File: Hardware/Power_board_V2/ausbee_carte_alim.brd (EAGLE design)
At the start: 97.1 x 71.4 mm, 27 parts, among them K1 G5LE

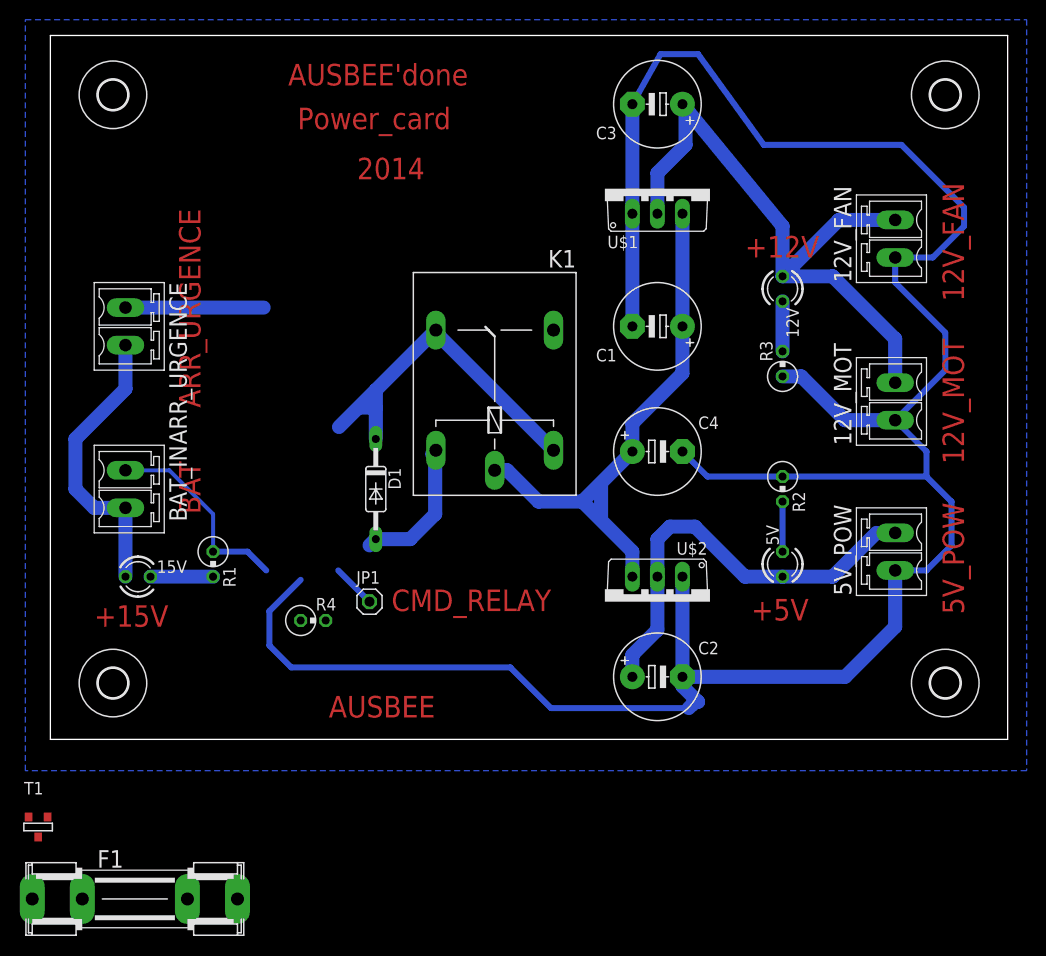
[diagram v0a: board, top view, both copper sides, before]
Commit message: Power board V2, adaptator GPIO
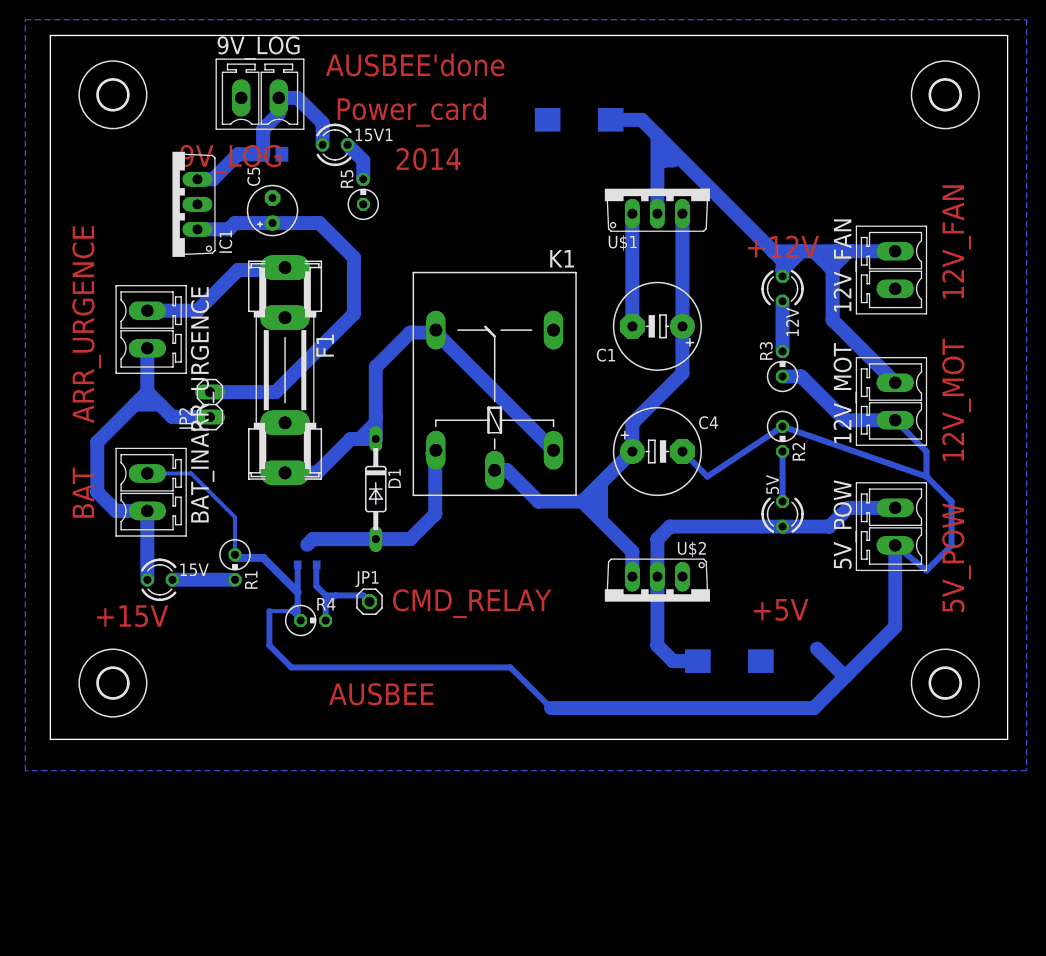
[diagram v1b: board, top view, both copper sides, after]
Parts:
- added 15V1: (no value), led:LED3MM
- added 9V_LOG: MCV2, con-phoenix-381_l:MCV2
- added C5: 0.33u, rcl:E2,5-5
- added C6: 100n, rcl:C0805
- added IC1: 7805TV, linear:TO220V
- added JP2: (no value), pinhead:1X02
- added R5: 470, rcl:0309V
- C2, C3: device rcl:E5-8,5 -> rcl:CT7343
- R3: value 870 -> 820
- moved F1 55.8 mm to (23.8, 37.5), turned to 270 degrees
- moved T1 38.8 mm to (26.0, 18.7), flipped to the bottom, turned to 180 degrees
- moved C3 8.09 mm to (53.7, 62.9), flipped to the bottom, turned to 0 degrees
- moved C2 7.47 mm to (68.9, 7.94), flipped to the bottom, turned to 180 degrees
- moved R2 5.08 mm to (74.3, 30.5)
- moved 5V 5.08 mm to (74.3, 22.9)
- moved 12V_FAN 3.17 mm to (85.7, 47.6)
- moved 5V_POW 2.54 mm to (85.7, 21.6)
- moved 15V 2.25 mm to (11.1, 16.2)
- moved R1 2.25 mm to (18.7, 17.5)
- moved BAT_IN 2.25 mm to (9.84, 25.1)
- moved ARR_URGENCE 2.25 mm to (9.84, 41.6)
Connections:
- new net +9V: 15V1.A, 9V_LOG.2, C6.1, IC1.3
- new net N$10: 15V1.K, R5.2
- new net N$9: C5.+, IC1.1, JP2.2
- net +15V: now also JP2.1
- net GND: now also 9V_LOG.1, C5.-, C6.2, IC1.2, R5.1
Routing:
- net GND: track 276.8 -> 193.9 mm
- net N$9: track 0.00 -> 41.2 mm
- net +9V: track 0.00 -> 21.8 mm
- net OUT_FUSE: track 37.3 -> 47.7 mm
- net +15V: track 29.6 -> 39.5 mm
- net N$6: track 4.49 -> 11.7 mm
- net N$5: track 15.0 -> 21.3 mm
- net N$10: track 0.00 -> 4.15 mm
- net +12V: track 65.8 -> 68.5 mm
- net +5V: track 43.6 -> 41.0 mm
- net N$11: track 0.00 -> 1.91 mm
- net OUT_ARR_URGENCE: track 14.0 -> 15.8 mm
- net N$8: track 0.00 -> 1.27 mm
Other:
- board text added: "9V_LOG"
